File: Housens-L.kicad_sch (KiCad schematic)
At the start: 48 parts, among them J1 JTAG/SWD, J2 USB_C_2.0, SW1 RESET, SW2 USER, U1 MCP1603, U2 BME280, U3 OPT3005, U4 STM32WB55CGUx, U5 STCC4, U6 REG710NA-3.3, U7 AP22966, U8 MLPF-WB55-01E3, Y1 32MHz, Y2 32.768kHz

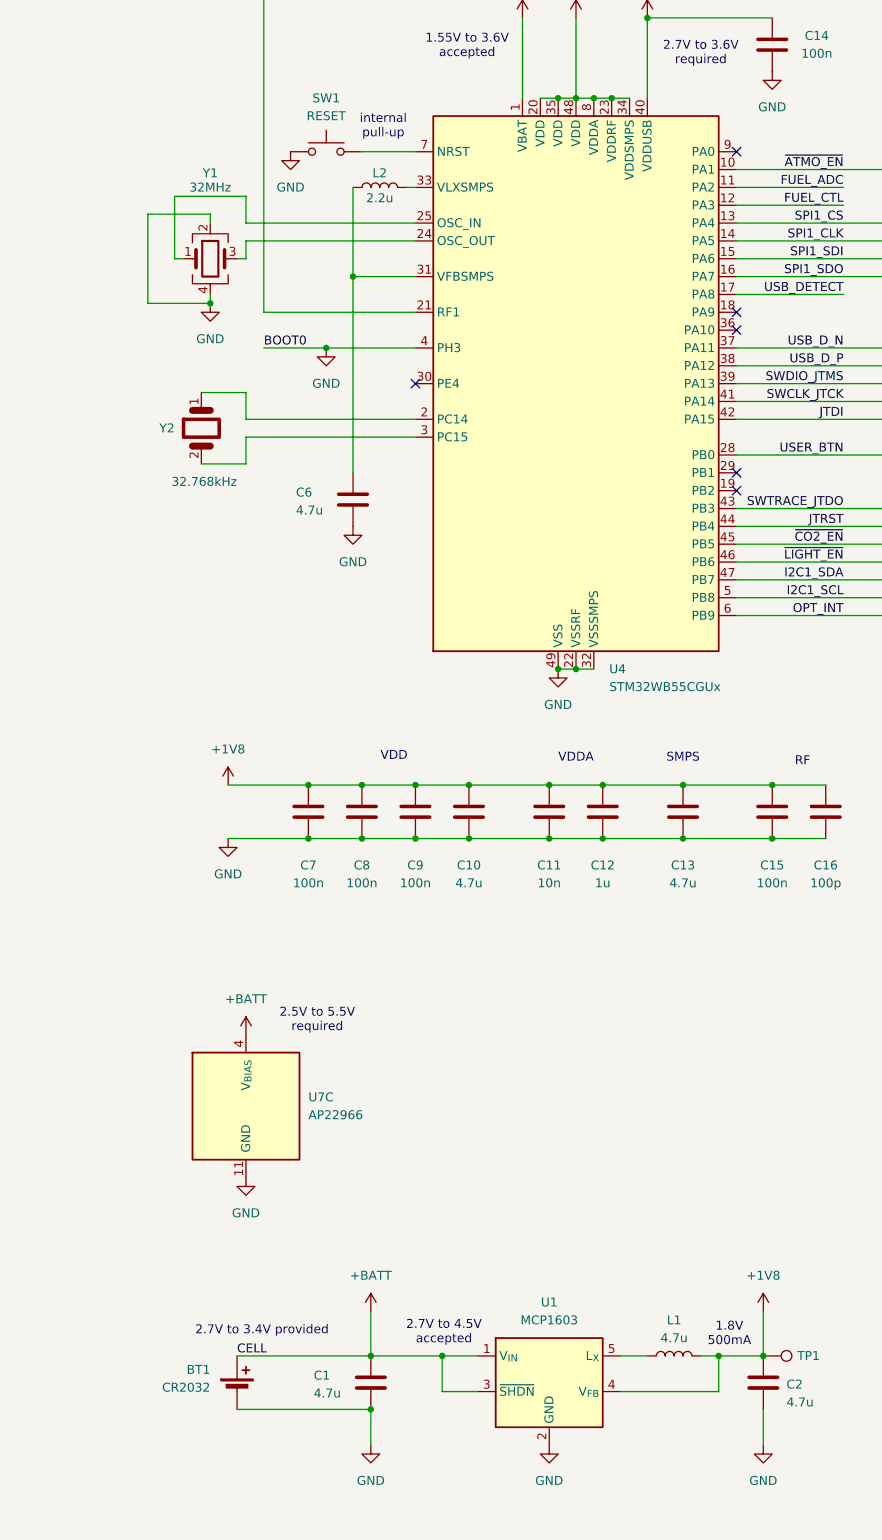
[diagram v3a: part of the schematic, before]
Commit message: Use LM voltage reg instead of unobtainium MCP
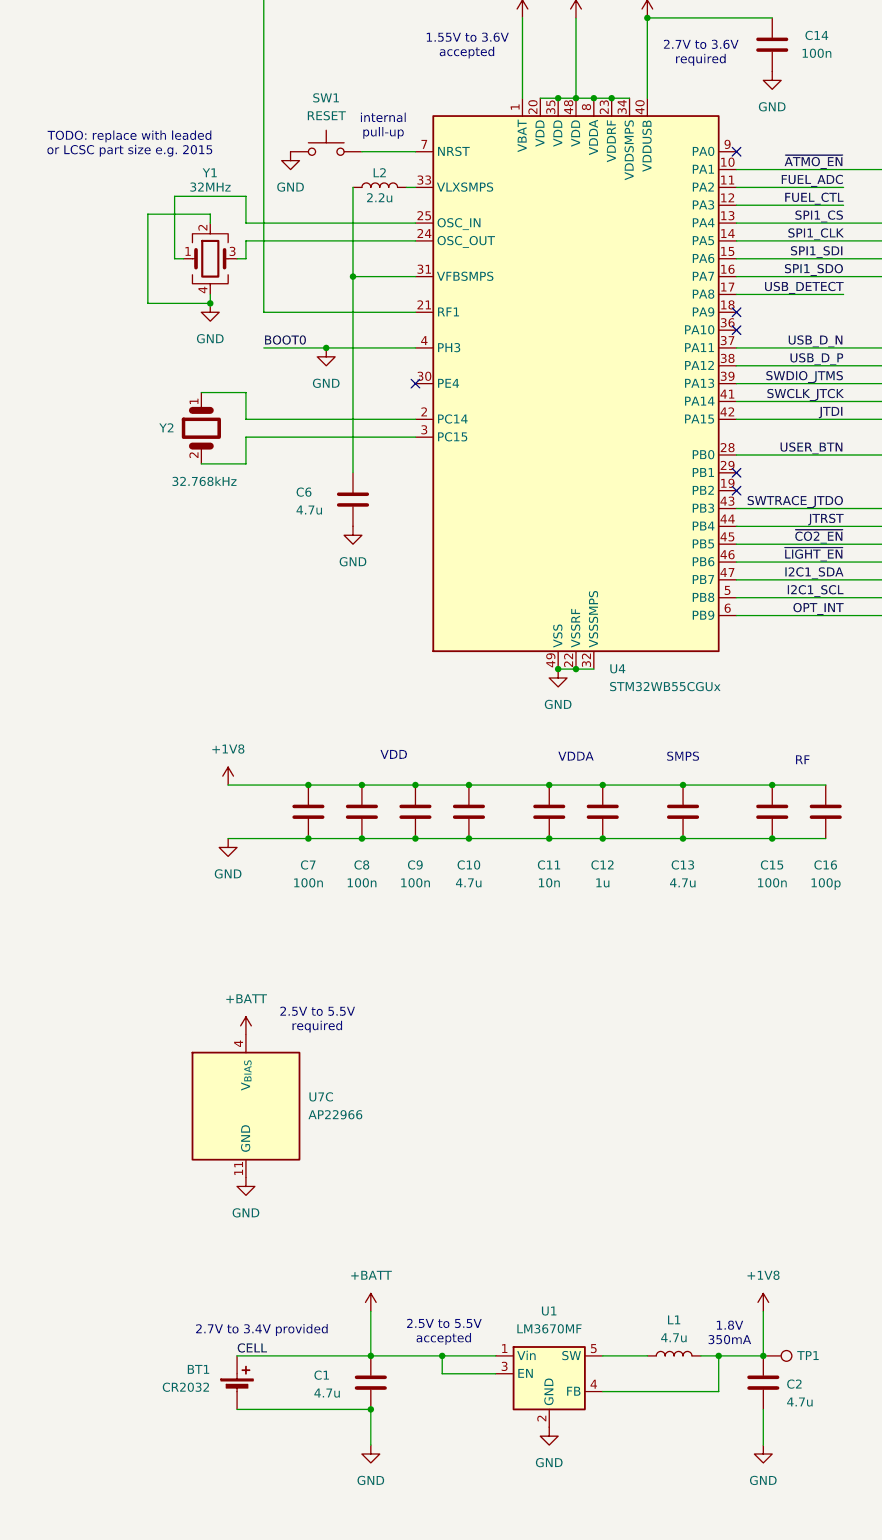
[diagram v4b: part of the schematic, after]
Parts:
- removed U1: MCP1603, Package_TO_SOT_SMD:SOT-23-5, symbol Imported:MCP1603
- added U1: LM3670MF, Package_TO_SOT_SMD:TSOT-23-5, symbol Regulator_Switching:LM3670MF
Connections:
- net +1V8: now also U1.4 (FB)
- net +BATT: now also U1.1 (Vin), U1.3 (EN)
- net GND: now also U1.2 (GND)
- net at L1.1: now also U1.5 (SW)
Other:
- note added: "1.8V 350mA"
- note added: "2.5V to 5.5V accepted"
- note added: "TODO: replace with leaded or LCSC part size e.g. 2015"
- note removed: "1.8V 500mA"
- note removed: "2.7V to 4.5V accepted"
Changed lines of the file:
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@@
 	(wire
 		(pts
-			(xy 60.96 257.81) (xy 60.96 252.73)
+			(xy 60.96 255.27) (xy 60.96 252.73)
 		)
 		(stroke
@@
 	(wire
 		(pts
-			(xy 66.04 257.81) (xy 60.96 257.81)
+			(xy 60.96 255.27) (xy 68.58 255.27)
 		)
 		(stroke
@@
 	(wire
 		(pts
+			(xy 83.82 252.73) (xy 90.17 252.73)
+		)
+		(stroke
+			(width 0)
+			(type default)
+		)
+	)
+	(wire
+		(pts
 			(xy 232.41 54.61) (xy 209.55 54.61)
 		)
@@
 	(wire
 		(pts
-			(xy 60.96 252.73) (xy 66.04 252.73)
+			(xy 60.96 252.73) (xy 68.58 252.73)
 		)
 		(stroke
@@
 	(wire
 		(pts
+			(xy 83.82 257.81) (xy 100.33 257.81)
+		)
+		(stroke
+			(width 0)
+			(type default)
+		)
+	)
+	(wire
+		(pts
 			(xy 49.53 179.07) (xy 57.15 179.07)
 		)
@@
 	(wire
 		(pts
-			(xy 86.36 252.73) (xy 90.17 252.73)
-		)
-		(stroke
-			(width 0)
-			(type default)
-		)
-	)
-	(wire
-		(pts
 			(xy 33.02 119.38) (xy 57.15 119.38)
 		)
@@
 	(wire
 		(pts
-			(xy 86.36 257.81) (xy 100.33 257.81)
-		)
-		(stroke
-			(width 0)
-			(type default)
-		)
-	)
-	(wire
-		(pts
 			(xy 179.07 139.7) (xy 179.07 140.97)
 		)
@@
 		)
 	)
-	(text "2.7V to 4.5V\naccepted"
+	(text "2.5V to 5.5V\naccepted"
 		(exclude_from_sim no)
 		(at 61.214 249.428 0)
@@
 		)
 	)
+	(text "TODO: replace with leaded\nor LCSC part size e.g. 2015"
+		(exclude_from_sim no)
+		(at 16.51 80.264 0)
+		(effects
+			(font
+				(size 1.27 1.27)
+			)
+		)
+	)
 	(text "2.7V to 3.4V\nprovided"
 		(exclude_from_sim no)
@@
 		)
 	)
-	(text "1.8V\n500mA"
+	(text "1.8V\n350mA"
 		(exclude_from_sim no)
 		(at 101.854 249.682 0)
@@
 	)
 	(symbol
-		(lib_id "Imported:MCP1603")
-		(at 76.2 257.81 0)
-		(unit 1)
-		(exclude_from_sim no)
-		(in_bom yes)
-		(on_board yes)
-		(dnp no)
-		(fields_autoplaced yes)
-		(property "Reference" "U1"
-			(at 76.2 245.11 0)
-			(effects
-				(font
-					(size 1.27 1.27)
-				)
-			)
-		)
-		(property "Value" "MCP1603"
-			(at 76.2 247.65 0)
-			(effects
-				(font
-					(size 1.27 1.27)
-				)
-			)
-		)
-		(property "Footprint" "Package_TO_SOT_SMD:SOT-23-5"
-			(at 77.47 264.16 0)
-			(effects
-				(font
-					(size 1.27 1.27)
-				)
-				(justify left)
-				(hide yes)
-			)
-		)
-		(property "Datasheet" "https://ww1.microchip.com/downloads/en/DeviceDoc/22042B.pdf"
-			(at 76.2 245.11 0)
-			(effects
-				(font
-					(size 1.27 1.27)
-				)
-				(hide yes)
-			)
-		)
-		(property "Description" "Synchronous Buck Regulator, VDD +2.7V to 5.5V, Out +1.8V, SOT-23"
-			(at 79.756 242.062 0)
-			(effects
-				(font
-					(size 1.27 1.27)
-				)
-				(hide yes)
-			)
-		)
-		(pin "2"
-		)
-		(pin "3"
-		)
-		(pin "1"
-		)
-		(pin "4"
-		)
-		(pin "5"
-		)
-		(instances
-			(project ""
-				(path "/36bb4837-104c-4aa4-b300-0e6d0ff24db5"
-					(reference "U1")
-					(unit 1)
-				)
-			)
-		)
-	)
-	(symbol
 		(lib_id "Device:C")
 		(at 232.41 71.12 0)
@@
 	)
 	(symbol
+		(lib_id "Regulator_Switching:LM3670MF")
+		(at 76.2 255.27 0)
+		(unit 1)
+		(exclude_from_sim no)
+		(in_bom yes)
+		(on_board yes)
+		(dnp no)
+		(fields_autoplaced yes)
+		(property "Reference" "U1"
+			(at 76.2 246.38 0)
+			(effects
+				(font
+					(size 1.27 1.27)
+				)
+			)
+		)
+		(property "Value" "LM3670MF"
+			(at 76.2 248.92 0)
+			(effects
+				(font
+					(size 1.27 1.27)
+				)
+			)
+		)
+		(property "Footprint" "Package_TO_SOT_SMD:TSOT-23-5"
+			(at 77.47 261.62 0)
+			(effects
+				(font
+					(size 1.27 1.27)
+				)
+				(justify left)
+				(hide yes)
+			)
+		)
+		(property "Datasheet" "http://www.ti.com/lit/ds/symlink/lm3670.pdf"
+			(at 69.85 264.16 0)
+			(effects
+				(font
+					(size 1.27 1.27)
+				)
+				(hide yes)
+			)
+		)
+		(property "Description" "Miniature Step-Down DC-DC Converter for Ultralow Voltage Circuits, 2.5V < Vin < 5.5V, adjustable output voltage, SOT-23-5"
+			(at 76.2 255.27 0)
+			(effects
+				(font
+					(size 1.27 1.27)
+				)
+				(hide yes)
+			)
+		)
+		(property "Part" "LM3670MFX-1.8/NOPB "
+			(at 76.2 255.27 0)
+			(effects
+				(font
+					(size 1.27 1.27)
+				)
+				(hide yes)
+			)
+		)
+		(pin "4"
+		)
+		(pin "5"
+		)
+		(pin "1"
+		)
+		(pin "2"
+		)
+		(pin "3"
+		)
+		(instances
+			(project ""
+				(path "/36bb4837-104c-4aa4-b300-0e6d0ff24db5"
+					(reference "U1")
+					(unit 1)
+				)
+			)
+		)
+	)
+	(symbol
 		(lib_id "Device:C")
 		(at 41.91 175.26 0)
@@
 	(symbol
 		(lib_id "power:GND")
-		(at 76.2 265.43 0)
+		(at 76.2 262.89 0)
 		(unit 1)
 		(exclude_from_sim no)
@@
 		(fields_autoplaced yes)
 		(property "Reference" "#PWR02"
-			(at 76.2 271.78 0)
+			(at 76.2 269.24 0)
 			(effects
 				(font
@@
 		)
 		(property "Value" "GND"
-			(at 76.2 270.51 0)
+			(at 76.2 267.97 0)
 			(effects
 				(font
@@
 		)
 		(property "Footprint" ""
-			(at 76.2 265.43 0)
+			(at 76.2 262.89 0)
 			(effects
 				(font
@@
 		)
 		(property "Datasheet" ""
-			(at 76.2 265.43 0)
+			(at 76.2 262.89 0)
 			(effects
 				(font
@@
 		)
 		(property "Description" "Power symbol creates a global label with name \"GND\" , ground"
-			(at 76.2 265.43 0)
+			(at 76.2 262.89 0)
 			(effects
 				(font

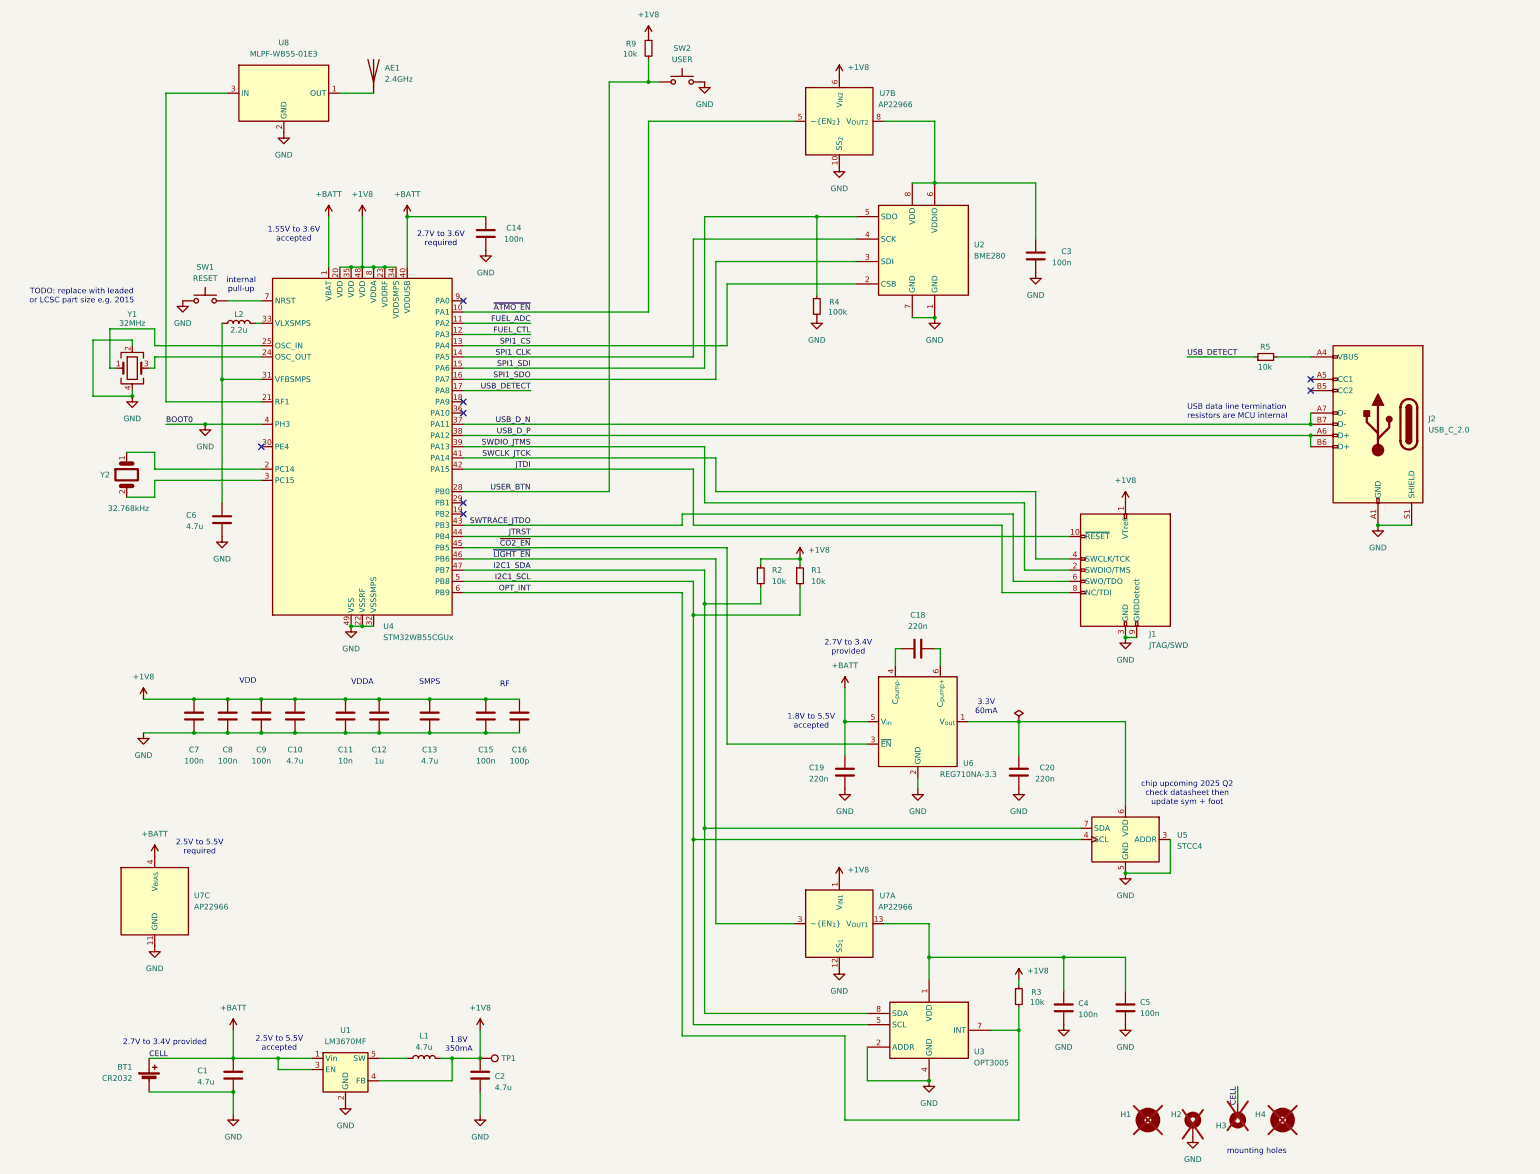
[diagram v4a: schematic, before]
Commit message: Add RPi-style debug port
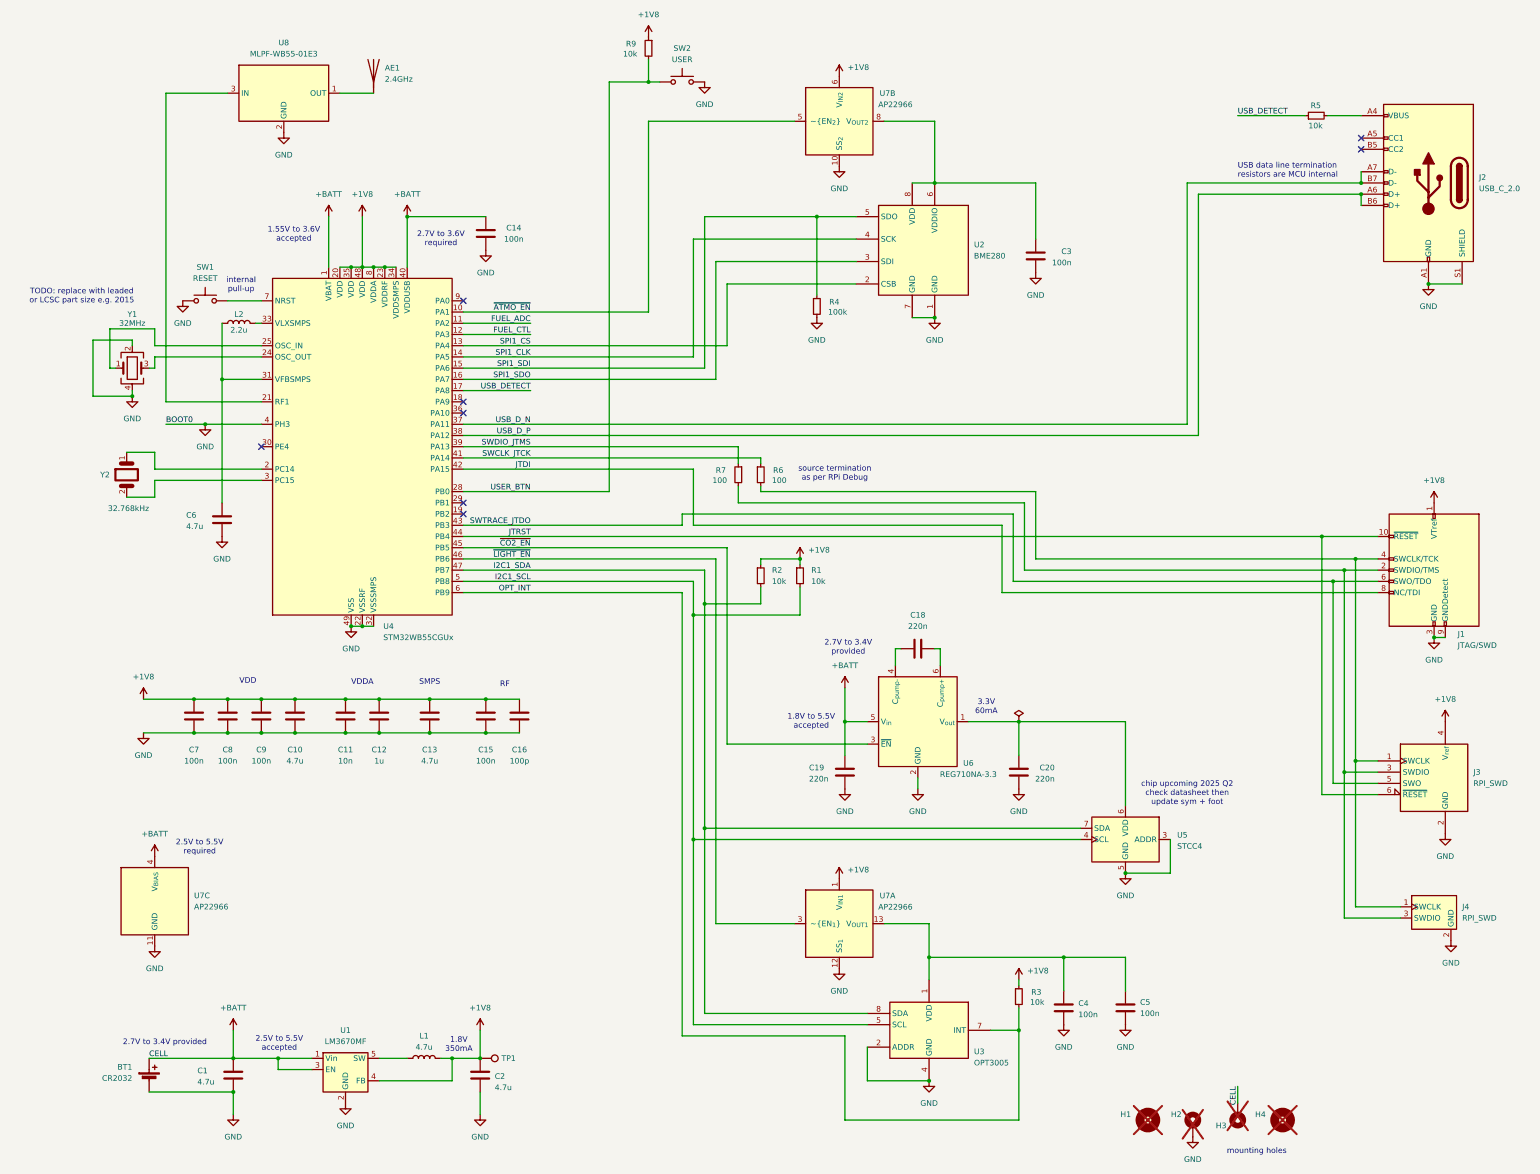
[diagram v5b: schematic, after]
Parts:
- added J3: RPI_SWD, Connector:Tag-Connect_TC2030-IDC-NL_2x03_P1.27mm_Vertical, symbol Invented:RPI_Debug_TC2030
- added J4: RPI_SWD, Connector_JST:JST_SH_SM03B-SRSS-TB_1x03-1MP_P1.00mm_Horizontal, symbol Invented:RPI_Debug_JST_SH
- added R6, R7: 100, Resistor_SMD:R_0603_1608Metric, symbol Device:R_Small
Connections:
- net +1V8: now also J3.4 (V_{ref})
- net GND: now also J3.2 (GND), J4.2 (GND)
- net JTRST: now also J3.6 (~{RESET})
- net SWCLK_JTCK: now also R6.1; no longer J1.4 (SWCLK/TCK)
- net SWDIO_JTMS: now also R7.1; no longer J1.2 (SWDIO/TMS)
- net SWTRACE_JTDO: now also J3.5 (SWO)
- new net: J1.4 (SWCLK/TCK), J3.1 (SWCLK), J4.1 (SWCLK), R6.2
- new net: J1.2 (SWDIO/TMS), J3.3 (SWDIO), J4.3 (SWDIO), R7.2
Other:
- note added: "source termination as per RPi Debug"
- moved on the sheet: J1, J2, R5
